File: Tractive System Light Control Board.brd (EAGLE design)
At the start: 88.9 x 50.8 mm, 63 parts, among them J1 MOLEX_CLICKMATE-2-VERTICAL, J2 MOLEX_CLICKMATE-2-VERTICAL, J3 MOLEX_CLICKMATE-2-VERTICAL, J4 MOLEX_CLICKMATE-2-VERTICAL, T1 750313734, T3 LMC555, U1 ISO7221, U12 SN6501DBVR, U2 TPS562219, U3 SN74LVC1G00DRL, U36 LTC1155, U37 CSD17506Q5A, U4 LM139, U5 MAX6168AESA+

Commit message: Added missing pad connections on high volt side,
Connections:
- net N$5: now also J4.2; no longer J4.1
- net N$6: now also J3.1; no longer J3.2
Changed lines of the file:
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@@
 <contactref element="C13" pad="2"/>
 <contactref element="R23" pad="2"/>
-<contactref element="J2" pad="1"/>
 <contactref element="R6" pad="P$2"/>
 <via x="16.51" y="44.45" extent="1-16" drill="0.6"/>
@@
 <wire x1="18.415" y1="2.54" x2="18.415" y2="3.54" width="0.4064" layer="1"/>
 <wire x1="18.415" y1="3.54" x2="18.685" y2="3.81" width="0.4064" layer="1"/>
+<contactref element="J2" pad="1"/>
 </signal>
 <signal name="HV_INDICATOR_SIGNAL_HV">
@@
 </signal>
 <signal name="N$5">
-<contactref element="J4" pad="1"/>
 <contactref element="R1" pad="P$2"/>
 <polygon width="0.4064" layer="1">
@@
 <vertex x="36.195" y="40.005"/>
 </polygon>
+<contactref element="J4" pad="2"/>
 </signal>
 <signal name="B+">
@@
 </signal>
 <signal name="N$6">
-<contactref element="J3" pad="2"/>
 <contactref element="R6" pad="P$1"/>
 <polygon width="0.4064" layer="1">
@@
 <vertex x="3.175" y="40.005"/>
 </polygon>
+<contactref element="J3" pad="1"/>
 </signal>
 <signal name="0.9V_REF">

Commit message: Added second pin connection to hv connections, regnerated gerbers
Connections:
- net B+: now also J1.1
- net GND1: now also J2.2
- net N$5: now also J4.1
- net N$6: now also J3.2
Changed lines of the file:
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@@
 <?xml version="1.0" encoding="utf-8"?>
 <!DOCTYPE eagle SYSTEM "eagle.dtd">
-<eagle version="7.5.0">
+<eagle version="7.3.0">
 <drawing>
 <settings>
@@
 <wire x1="18.415" y1="3.54" x2="18.685" y2="3.81" width="0.4064" layer="1"/>
 <contactref element="J2" pad="1"/>
+<contactref element="J2" pad="2"/>
 </signal>
 <signal name="HV_INDICATOR_SIGNAL_HV">
@@
 </polygon>
 <contactref element="J4" pad="2"/>
+<contactref element="J4" pad="1"/>
 </signal>
 <signal name="B+">
@@
 <vertex x="27.305" y="36.195"/>
 </polygon>
+<contactref element="J1" pad="1"/>
 </signal>
 <signal name="N$6">
@@
 </polygon>
 <contactref element="J3" pad="1"/>
+<contactref element="J3" pad="2"/>
 </signal>
 <signal name="0.9V_REF">

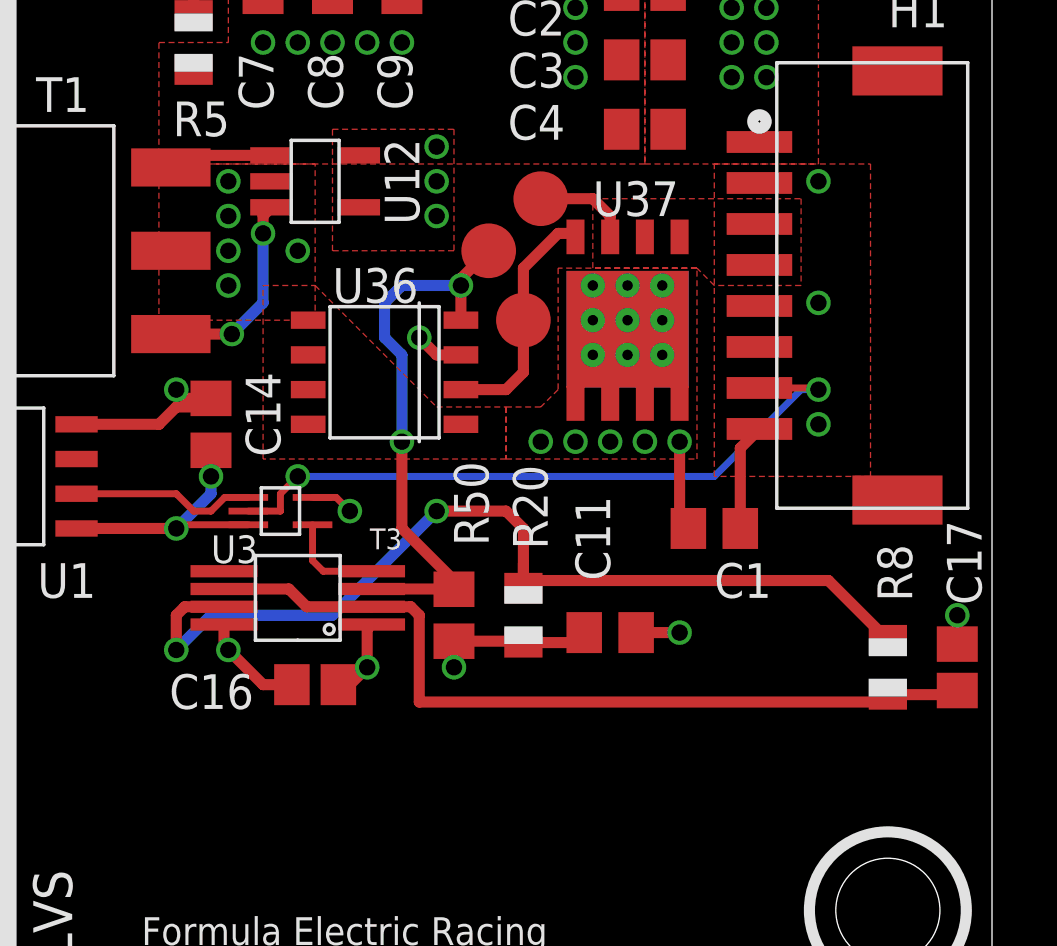
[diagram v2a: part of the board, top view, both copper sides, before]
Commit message: Added discharge relay driver, regen gerbers
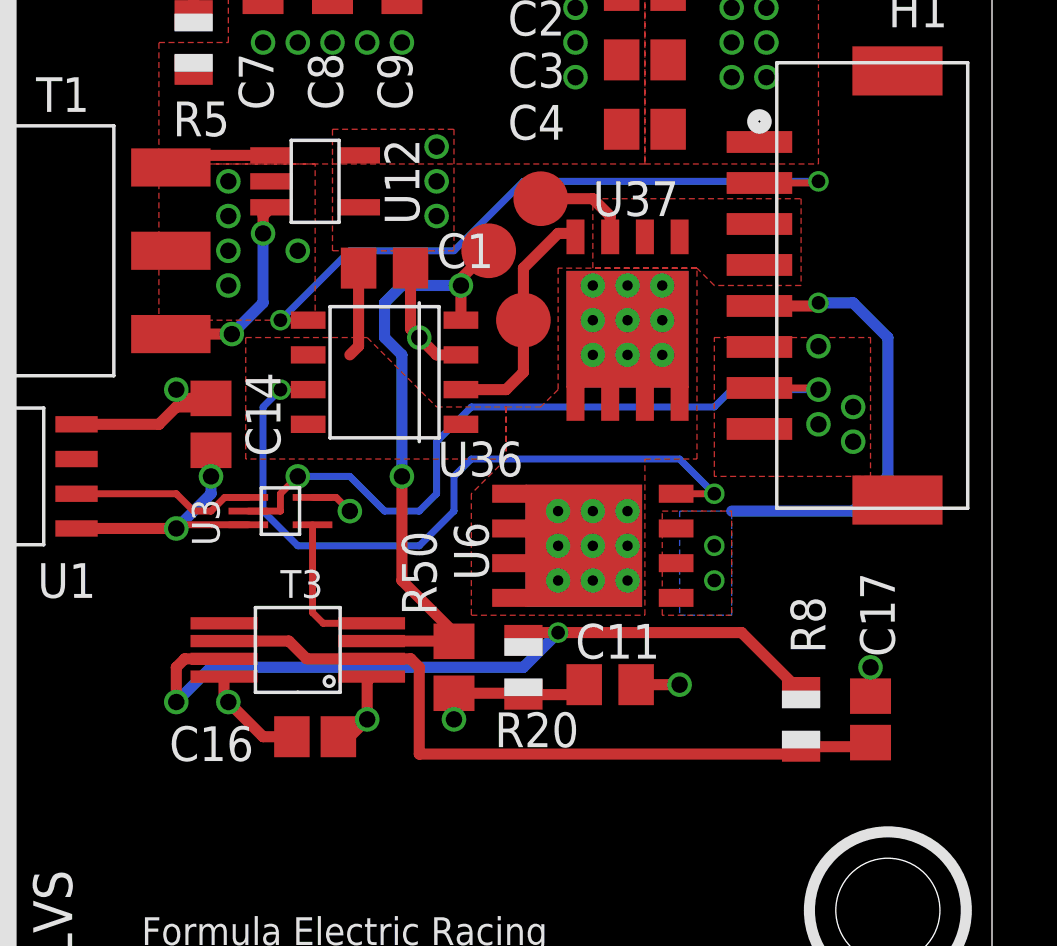
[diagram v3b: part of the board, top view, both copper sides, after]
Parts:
- added U6: CSD17506Q5A, FormE:SON_5X6
- moved C1 15.4 mm to (66.7, 27.3)
- moved C17 3.70 mm to (84.5, 10.8)
- moved R8 3.70 mm to (81.9, 10.8)
- moved C11 1.91 mm to (74.9, 12.1)
- moved R20 1.91 mm to (71.8, 12.7)
- moved R50 1.91 mm to (69.2, 12.7)
- moved C16 1.90 mm to (64.1, 10.2)
- moved T3 1.90 mm to (63.5, 13.3)
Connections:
- new net CONTACTOR_OFF: H1.2, U36.5
- new net DISCHARGE_RELAY_OUT: H1.5, U6.1, U6.2, U6.3
- new net N$7: U36.7, U6.4
- net GND: now also H1.6; no longer H1.2, H1.5
- net VCC: now also U36.8, U6.5, U6.6, U6.7, U6.8, U6.PAD, U6.PAD1, U6.VIA1, U6.VIA2, U6.VIA3, U6.VIA4, U6.VIA5, U6.VIA6, U6.VIA7, U6.VIA8, U6.VIA9
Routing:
- net N$7: track 0.00 -> 26.7 mm, vias 0 -> 2
- net CONTACTOR_OFF: track 0.00 -> 25.0 mm, vias 0 -> 2
- net DISCHARGE_RELAY_OUT: track 0.00 -> 16.6 mm, vias 0 -> 3
- net N$12: track 35.6 -> 29.3 mm
- net N$13: track 30.6 -> 27.4 mm
- net AIR_CLOSED: track 25.3 -> 27.4 mm
- net 555_TIMER_CONTROL: track 3.63 -> 5.54 mm
- net 555_TIMER_OUTPUT: track 20.6 -> 22.5 mm
- net GND: track 24.9 -> 23.7 mm, vias 25 -> 26
- net VCC: vias 12 -> 7
- added copper zone on layer 1, net DISCHARGE_RELAY_OUT
- added copper zone on layer 16, net DISCHARGE_RELAY_OUT
